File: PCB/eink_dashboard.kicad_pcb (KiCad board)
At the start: 2 copper layers, 64.5 x 55.4 mm, 60 parts, among them J1 USB_B_Micro, J2 Conn_01x05, Q1 IRLML6402, Q2 IRLML6402, Q3 IRLML6402, Q4 IRLML6402, U1 LM358, U10 CD4094, U11 CD4094, U2 MCP73831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

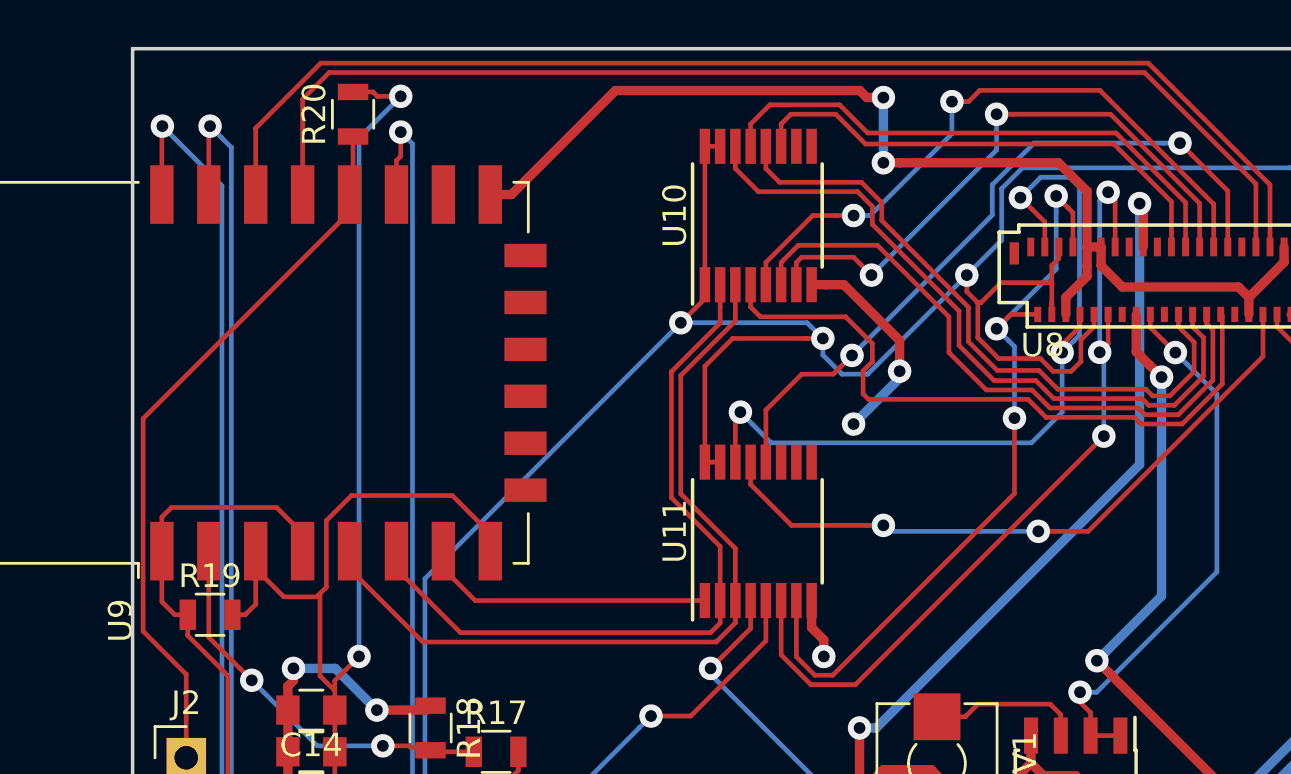
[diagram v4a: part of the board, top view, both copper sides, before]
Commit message: Ground pours tweaked
Added pour keepout areas (F.Cu) under ICs, inductors and FPC connector
Pour minimal width increased
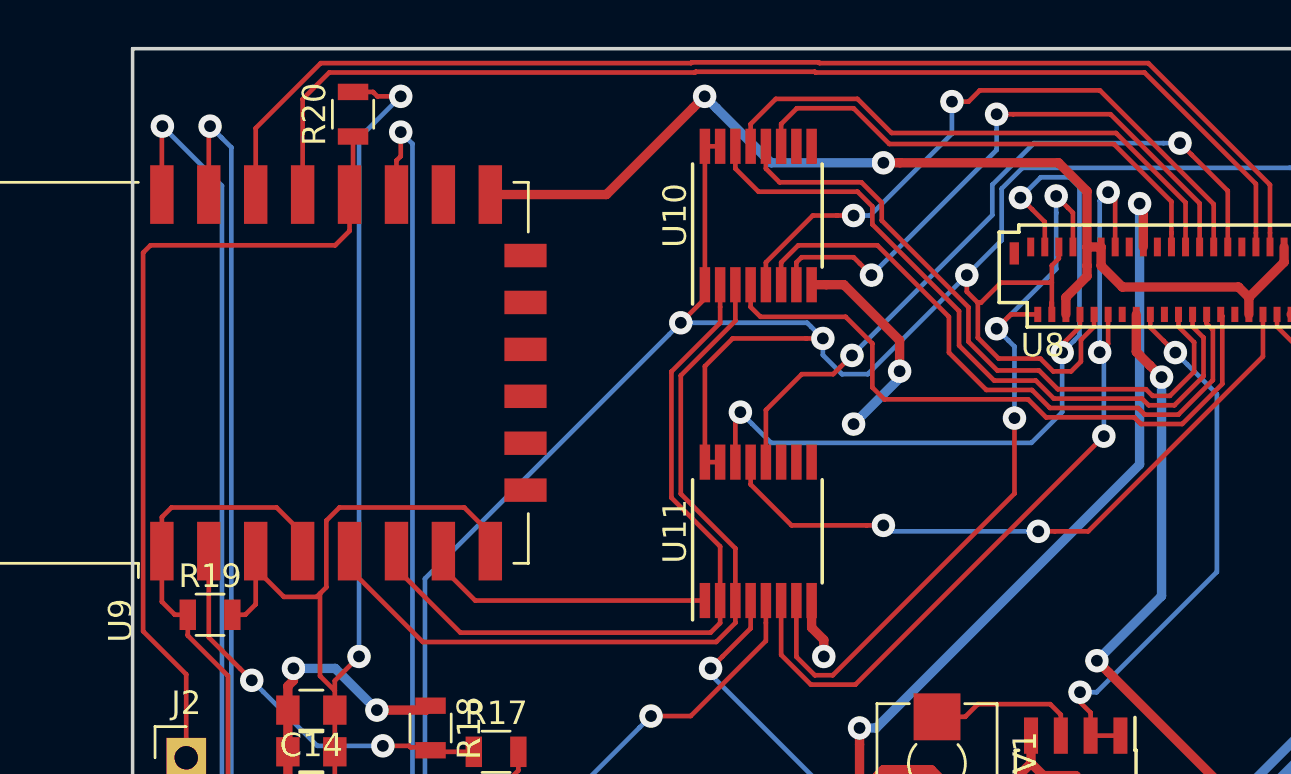
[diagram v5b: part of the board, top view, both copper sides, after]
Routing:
- net Net-(J2-Pad1): track 31.0 -> 36.4 mm
- net GND: track 226.3 -> 224.4 mm
- net Net-(U10-Pad4): track 28.6 -> 27.9 mm
